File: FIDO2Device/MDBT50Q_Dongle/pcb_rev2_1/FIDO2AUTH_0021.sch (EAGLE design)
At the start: 36 parts, among them CN1 TE-1734028, CN2 IF_4PIN, SW1 SKRPACE010, SW2 SKTADAE010, U1 MDBT50Q-P1M, U2 XC6206P332MR-G, U3 ATECC608A-MAHDA-S, X1 NX3215SA-32.768K

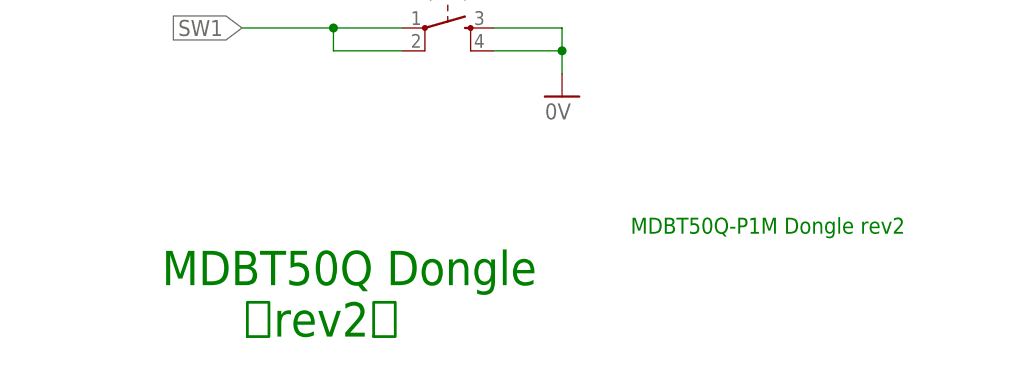
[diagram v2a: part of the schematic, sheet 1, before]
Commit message: ドキュメントを作成
・回路図、部品レイアウト図を出力
・回路図の名称を修正（rev2.1）
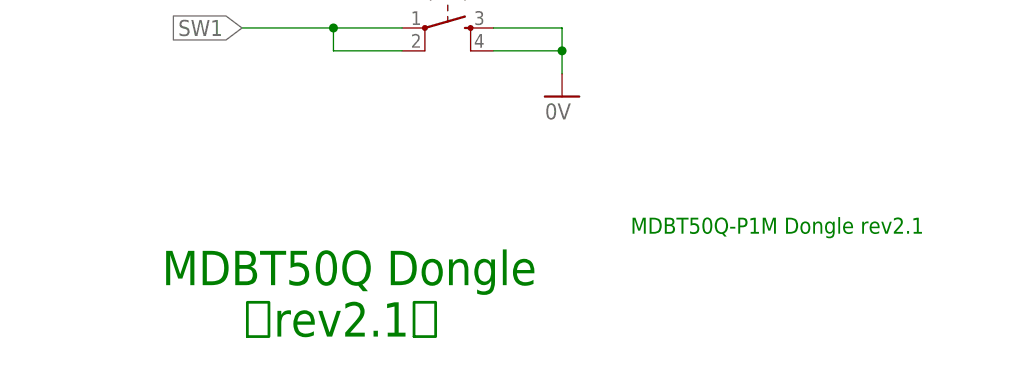
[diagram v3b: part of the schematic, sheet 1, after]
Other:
- note added: "MDBT50Q Dongle （rev2.1）"
- note added: "MDBT50Q-P1M Dongle rev2.1"
- note removed: "MDBT50Q Dongle （rev2）"
- note removed: "MDBT50Q-P1M Dongle rev2"
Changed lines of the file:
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@@
 <text x="152.4" y="152.4" size="2.54" layer="91">32.768kHzクリスタル</text>
 <text x="203.2" y="152.4" size="2.54" layer="91">バイパスコンデンサー</text>
-<text x="218.44" y="20.32" size="1.778" layer="91">MDBT50Q-P1M Dongle rev2</text>
+<text x="218.44" y="20.32" size="1.778" layer="91">MDBT50Q-P1M Dongle rev2.1</text>
 <text x="166.37" y="8.89" size="3.81" layer="91">MDBT50Q Dongle
-      （rev2）</text>
+      （rev2.1）</text>
 <text x="20.32" y="162.56" size="3.81" layer="91">モジュール部</text>
 <text x="167.64" y="91.44" size="2.54" layer="91">リセット回路</text>
@@
 <text x="152.4" y="81.28" size="2.54" layer="91">USBブートローダーを
 書込する際に使用します。</text>
-<text x="218.44" y="20.32" size="1.778" layer="91">MDBT50Q-P1M Dongle rev2</text>
+<text x="218.44" y="20.32" size="1.778" layer="91">MDBT50Q-P1M Dongle rev2.1</text>
 <text x="166.37" y="8.89" size="3.81" layer="91">MDBT50Q Dongle
-      （rev2）</text>
+      （rev2.1）</text>
 <text x="124.46" y="66.04" size="2.54" layer="91">LED（黄色）</text>
 <text x="76.2" y="66.04" size="2.54" layer="91">LED（３色）</text>
@@
 <text x="78.74" y="60.96" size="2.54" layer="91">ボタン乾電池ケースは
 基板の背面に実装</text>
-<text x="218.44" y="20.32" size="1.778" layer="91">MDBT50Q-P1M Dongle rev2</text>
+<text x="218.44" y="20.32" size="1.778" layer="91">MDBT50Q-P1M Dongle rev2.1</text>
 <text x="166.37" y="8.89" size="3.81" layer="91">MDBT50Q Dongle
-      （rev2）</text>
+      （rev2.1）</text>
 </plain>
 <instances>
@@
 <sheet>
 <plain>
-<text x="218.44" y="20.32" size="1.778" layer="91">MDBT50Q-P1M Dongle rev2</text>
+<text x="218.44" y="20.32" size="1.778" layer="91">MDBT50Q-P1M Dongle rev2.1</text>
 <text x="166.37" y="8.89" size="3.81" layer="91">MDBT50Q Dongle
-      （rev2）</text>
+      （rev2.1）</text>
 <text x="45.72" y="134.62" size="3.81" layer="91">セキュリティーIC部</text>
 </plain>
